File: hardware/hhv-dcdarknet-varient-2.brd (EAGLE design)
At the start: 43.2 x 75.8 mm, 62 parts, among them IC1 ATMEGA328P-PU, U1 RCV, U2 VT1045CTO262-H, X2 USB

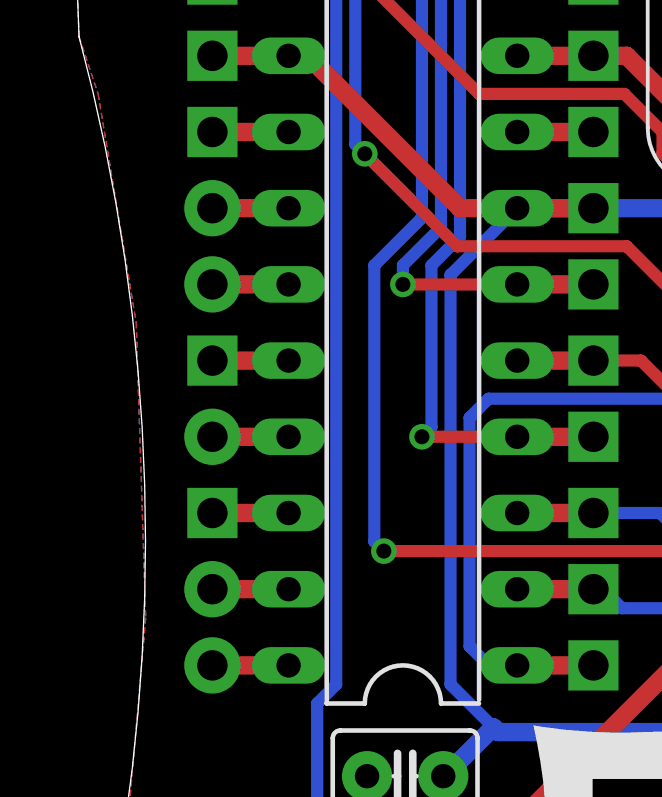
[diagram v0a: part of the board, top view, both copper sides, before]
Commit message: Updated Eagle files for the 2015 boards.
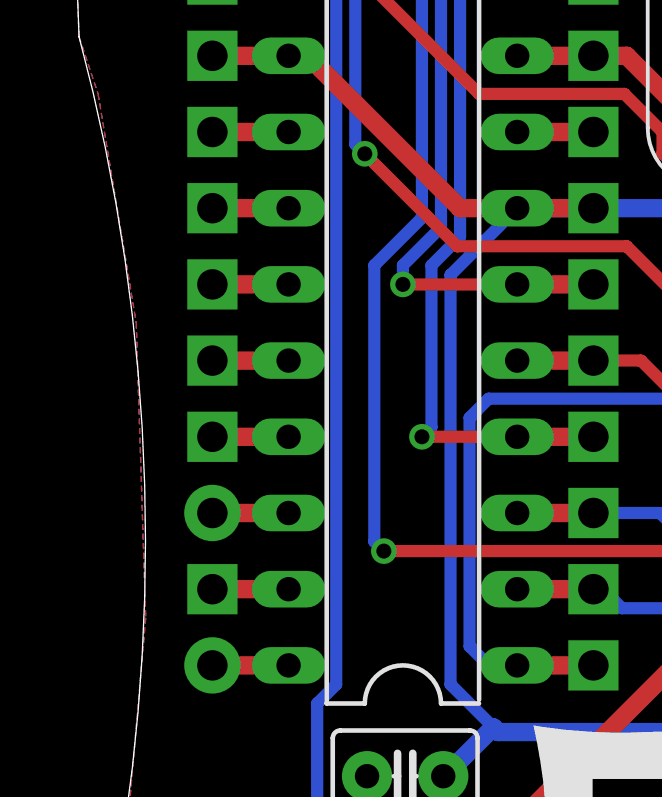
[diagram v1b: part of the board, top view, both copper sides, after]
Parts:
- JP24, JP25, JP27, JP29: device adafruit:1X1-SMALL -> adafruit:1X1-SMALL_CUT
- JP28: device adafruit:1X1-SMALL_CUT -> adafruit:1X1-SMALL
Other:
- board text added: "43102 16810 13248 93348"
- board text added: "56628 85115 30926 53950"
- board text added: "76821 71699 85378 99246"
- board text added: "94173 72223"
- board text removed: "17185 65867 58278 18586"
- board text removed: "48269 27789"
- board text removed: "69667 18282 71718 71667"
- board text removed: "86697 06566 65707 70677"
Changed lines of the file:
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@@
 <wire x1="56.515" y1="61.2775" x2="56.67375" y2="61.356875" width="0.6096" layer="41"/>
 <text x="46.99" y="52.3875" size="0.8128" layer="121" rot="R90">USB Tx</text>
-<text x="77.33665" y="8.226425" size="1.27" layer="122" font="vector" distance="45" rot="MR0">69667
-18282
-71718
-71667</text>
+<text x="77.33665" y="8.226425" size="1.27" layer="122" font="vector" distance="45" rot="MR0">76821
+71699
+85378
+99246</text>
 <wire x1="76.04125" y1="21.43125" x2="75.08875" y2="21.43125" width="0.254" layer="122"/>
 <wire x1="75.08875" y1="21.43125" x2="74.13625" y2="21.43125" width="0.254" layer="122"/>
@@
 <vertex x="62.865" y="52.3875"/>
 </polygon>
-<text x="70.8279" y="8.226425" size="1.27" layer="122" font="vector" distance="45" rot="MR0">17185
-65867
-58278
-18586</text>
-<text x="64.31915" y="8.226425" size="1.27" layer="122" font="vector" distance="45" rot="MR0">86697
-06566
-65707
-70677</text>
-<text x="57.8104" y="8.226425" size="1.27" layer="122" font="vector" distance="45" rot="MR0">48269
-27789</text>
+<text x="70.8279" y="8.226425" size="1.27" layer="122" font="vector" distance="45" rot="MR0">56628
+85115
+30926
+53950</text>
+<text x="64.31915" y="8.226425" size="1.27" layer="122" font="vector" distance="45" rot="MR0">43102
+16810
+13248
+93348</text>
+<text x="57.8104" y="8.226425" size="1.27" layer="122" font="vector" distance="45" rot="MR0">94173
+72223</text>
 </plain>
 <attributes>
@@
 <element name="JP22" library="adafruit" package="1X1-SMALL_CUT" value="" x="48.26" y="36.83"/>
 <element name="JP23" library="adafruit" package="1X1-SMALL_CUT" value="" x="48.26" y="34.29"/>
-<element name="JP24" library="adafruit" package="1X1-SMALL" value="" x="48.26" y="31.75"/>
-<element name="JP25" library="adafruit" package="1X1-SMALL" value="" x="48.26" y="29.21"/>
+<element name="JP24" library="adafruit" package="1X1-SMALL_CUT" value="" x="48.26" y="31.75"/>
+<element name="JP25" library="adafruit" package="1X1-SMALL_CUT" value="" x="48.26" y="29.21"/>
 <element name="JP26" library="adafruit" package="1X1-SMALL_CUT" value="" x="48.26" y="26.67"/>
-<element name="JP27" library="adafruit" package="1X1-SMALL" value="" x="48.26" y="24.13"/>
-<element name="JP28" library="adafruit" package="1X1-SMALL_CUT" value="" x="48.26" y="21.59"/>
-<element name="JP29" library="adafruit" package="1X1-SMALL" value="" x="48.26" y="19.05"/>
+<element name="JP27" library="adafruit" package="1X1-SMALL_CUT" value="" x="48.26" y="24.13"/>
+<element name="JP28" library="adafruit" package="1X1-SMALL" value="" x="48.26" y="21.59"/>
+<element name="JP29" library="adafruit" package="1X1-SMALL_CUT" value="" x="48.26" y="19.05"/>
 <element name="JP30" library="adafruit" package="1X1-SMALL" value="" x="48.26" y="16.51"/>
 <element name="C3" library="adafruit" package="C025-030X050" value=".1uf" x="75.40625" y="17.93875" smashed="yes" rot="R270">
@@
 </element>
 <element name="R7" library="SparkFun" package="1206" value="" x="83.185" y="63.8175" smashed="yes" rot="MR270">
-<attribute name="NAME" x="83.78825" y="66.548" size="0.8128" layer="26" rot="MR0"/>
+<attribute name="NAME" x="83.78825" y="66.38925" size="0.8128" layer="26" rot="MR0"/>
 <attribute name="VALUE" x="84.582" y="64.8335" size="0.4064" layer="28" rot="MR270"/>
 </element>
 <element name="R8" library="SparkFun" package="1206" value="" x="75.8825" y="66.675" smashed="yes" rot="MR270">
-<attribute name="NAME" x="74.58075" y="66.38925" size="0.8128" layer="26" rot="MR0"/>
+<attribute name="NAME" x="74.7395" y="66.2305" size="0.8128" layer="26" rot="MR0"/>
 <attribute name="VALUE" x="77.2795" y="67.691" size="0.4064" layer="28" rot="MR270"/>
 </element>
